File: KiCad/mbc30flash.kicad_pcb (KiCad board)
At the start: 2 copper layers, 51 x 60.2 mm, 19 parts, among them U0 CartBus, U1 BA6129AF, U2 74LVC1G332GW,125, Y1 Crystal

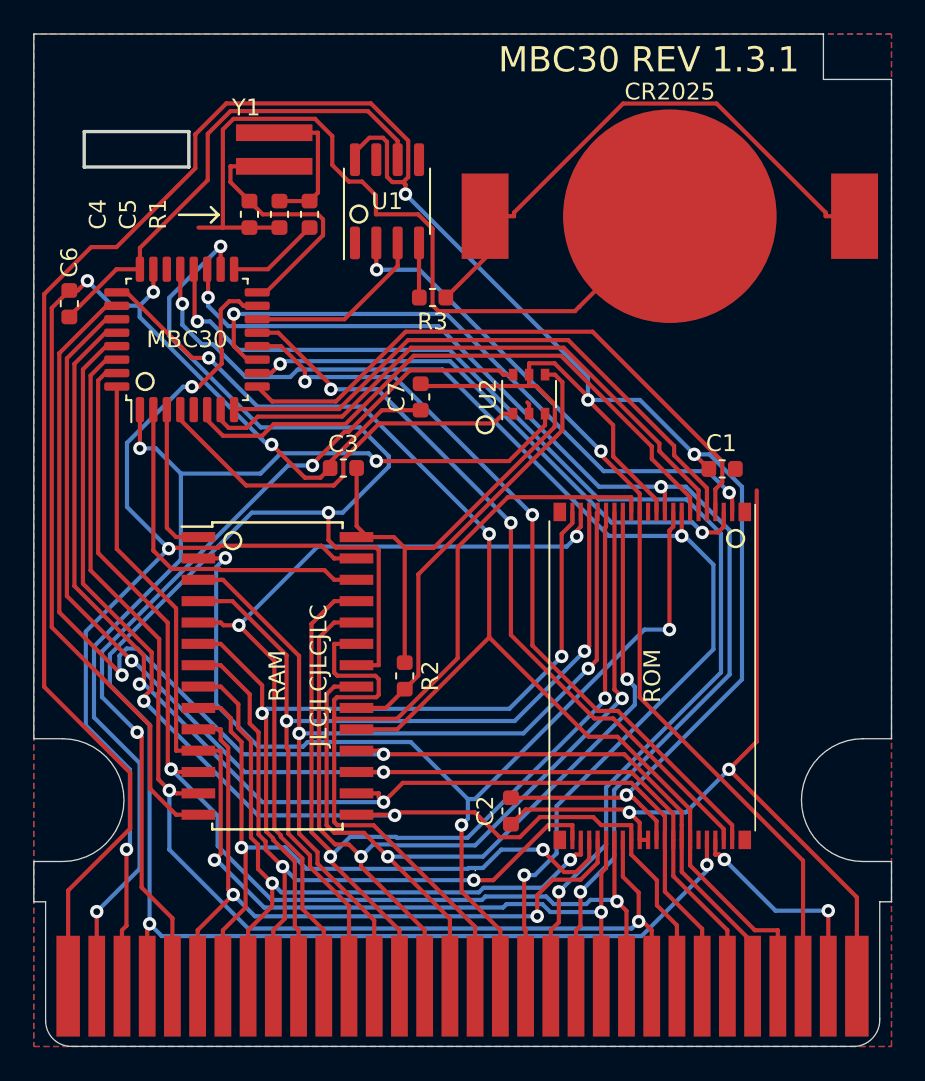
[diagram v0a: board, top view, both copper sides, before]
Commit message: Revision 1.4
- Switched cart bus footprint to [djedditt's replica of an original one](https://github.com/djedditt/kicad-gamepaks)

- Replaced the flash chip footprint with a TSOP-40 footprint.

- Redid the ground plane by hand, it should now look much better.

- Moved the battery receptacle footprint 0.5mm to the left.

- Renamed Y1 to X1

- Removed JLCJLCJLC marking for OSHPark project.

- Cleaned up schematic, it should now be much more readable.
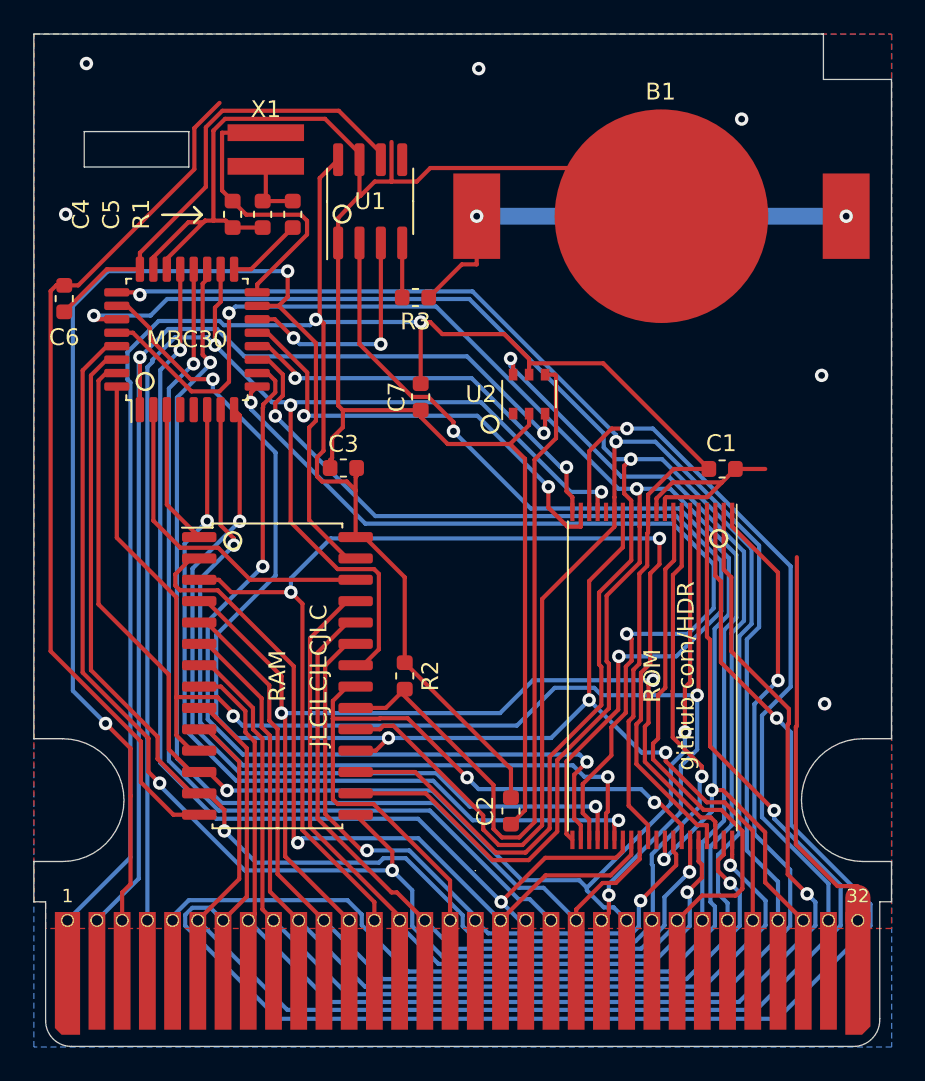
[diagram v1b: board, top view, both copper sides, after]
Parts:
- removed the ROM at (101.7, 108.0)
- removed Y1: Crystal, Custom:Resonator_SMD_muRata_CDSCB-2pin_4.5x2.0mm_HandSoldering
- added ROM: AM29F032/MBM29F033C, Custom:AM29F032-MBM29F033C, F.Cu at (101.7, 108.0)
- added X1: Crystal, Custom:Resonator_SMD_muRata_CDSCB-2pin_4.5x2.0mm_HandSoldering, F.Cu at (78.7, 76.7)
- R1: value 300Kohm -> 330K
- R2: value 10 Kohm -> 10K
- R3: value 1 Kohm -> 1K
- U0: footprint Custom:GBBus -> Connector_GameBoy:GameBoy_GamePak_CGB-002_P1.50mm_Edge
- moved G*** 31.9 mm to (90.4, 99.9)
- moved U0 24.3 mm to (90.4, 120.6)
- moved R3 1.02 mm to (87.6, 85.5)
- moved C4 1.00 mm to (76.7, 80.5)
- moved C5 1.00 mm to (78.5, 80.5)
- moved R1 1.00 mm to (80.3, 80.5)
- moved U1 1.00 mm to (84.9, 79.7)
- moved B1 0.50 mm to (102.2, 80.6)
- moved C6 0.43 mm to (66.7, 85.5)
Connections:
- MBC30 pad 4: \RAMCS -> Net-(U1-Pad4)
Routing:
- net A1: track 42.8 -> 91.8 mm, vias 2 -> 1
- net VCC: track 193.8 -> 151.4 mm, vias 4 -> 2
- net A0: track 43.4 -> 84.0 mm, vias 2 -> 1
- net A2: track 41.4 -> 80.7 mm, vias 2 -> 1
- net A3: track 42.1 -> 78.8 mm, vias 2 -> 1
- net D5: track 72.7 -> 109.3 mm
- net D4: track 72.6 -> 108.4 mm
- net D7: track 74.1 -> 107.9 mm
- net GND: track 168.4 -> 201.1 mm, vias 5 -> 6
- net D3: track 70.4 -> 101.1 mm
- net WE_AUDIO: track 13.5 -> 42.9 mm, vias 2 -> 1
- net \RD: track 116.5 -> 90.4 mm, vias 4 -> 3
- net CS: track 53.2 -> 79.2 mm, vias 2 -> 1
- net \RAMCS: track 24.4 -> 0.00 mm
- net RA20: track 46.1 -> 24.4 mm
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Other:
- board text added: "MBC30 REV 1.4"
- board text added: "github.com/HDR"
- board text removed: "CR2025"
- board text removed: "MBC30 REV 1.3.1"

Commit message: 1.4.1
- Fixed missing trace for Ram_CS
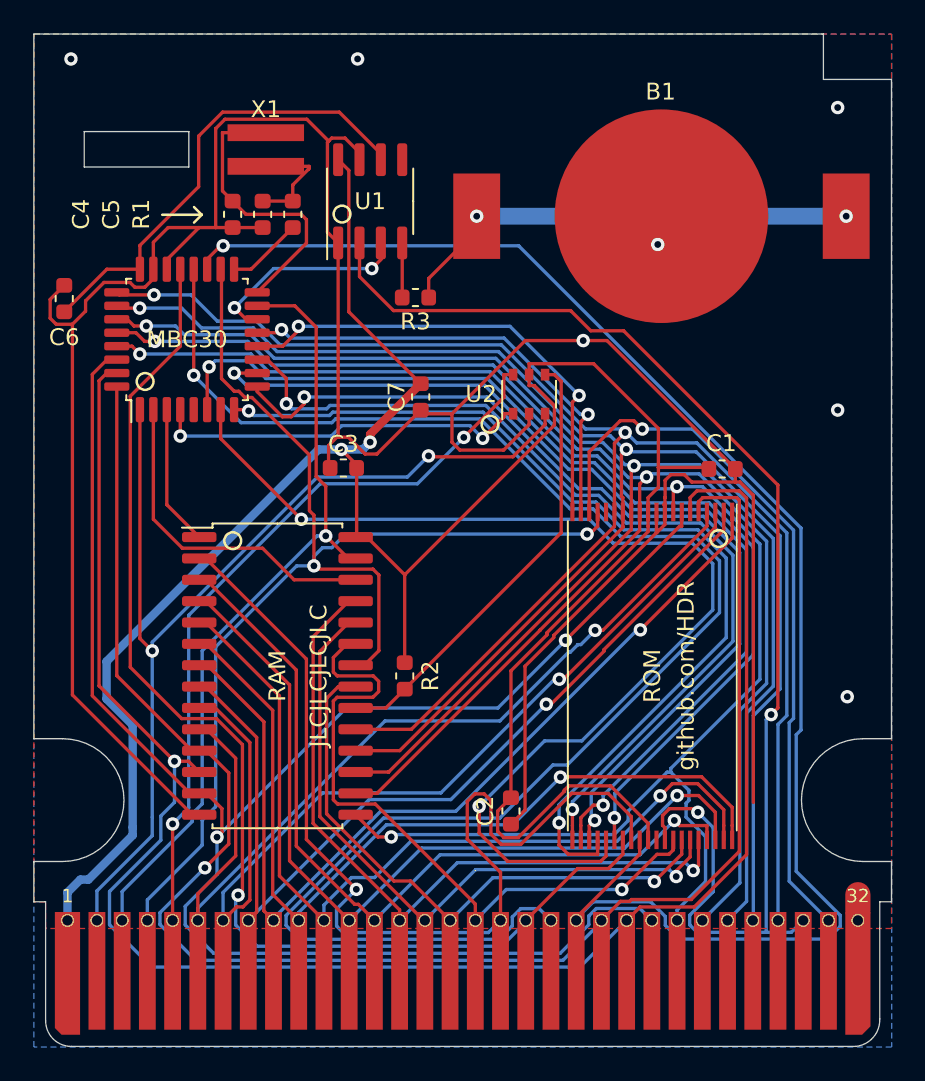
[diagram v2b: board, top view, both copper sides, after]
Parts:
- removed G***: LOGO, Custom:Suicune-Back-Silkscreen
- added Art2: 90,412581|99,90646 | Suicune, Custom:Suicune-Back-Silkscreen, B.Cu at (90.4, 99.9)
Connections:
- MBC30 pad 4: Net-(U1-Pad4) -> \RAMCS
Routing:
- net A14: track 56.5 -> 96.7 mm
- net A1: track 91.8 -> 56.2 mm
- net CS: track 79.2 -> 44.6 mm, vias 1 -> 2
- net A0: track 84.0 -> 54.7 mm
- net A15: track 64.7 -> 92.2 mm
- net A2: track 80.7 -> 54.8 mm
- net \WR: track 72.9 -> 47.2 mm, vias 2 -> 1
- net D1: track 81.4 -> 106.2 mm, vias 2 -> 1
- net A7: track 71.6 -> 48.1 mm, vias 2 -> 1
- net A3: track 78.8 -> 55.6 mm
- net \RAMCS: track 0.00 -> 22.7 mm, vias 0 -> 2
- net #CE: track 44.5 -> 26.7 mm
- net RA15: track 49.1 -> 66.5 mm
- net D2: track 88.8 -> 105.5 mm
- net D0: track 83.5 -> 99.1 mm, vias 3 -> 1
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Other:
- net class Default: trace_width 0.25 -> 0.2
- board text added: "MBC30 REV 1.4.1"
- board text removed: "MBC30 REV 1.4"

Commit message: 1.4.2
- Fixed a symbol kicad "rescued" causing the pinout to be backwards (this put the chip direction indicator in the wrong corner)
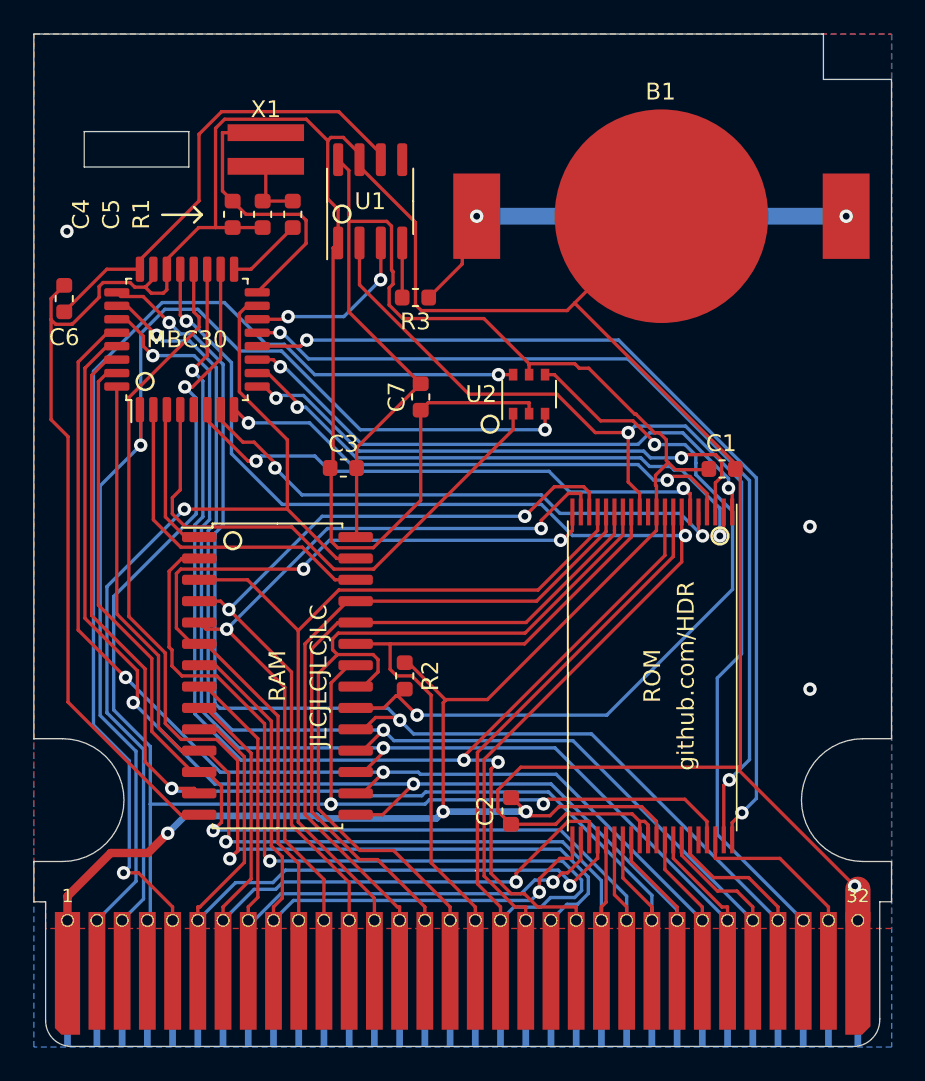
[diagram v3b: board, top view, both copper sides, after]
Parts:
- removed Art2: 90,412581|99,90646 | Suicune, Custom:Suicune-Back-Silkscreen
- added Art1: 90,412581|99,90646 | Crystal Clear, Custom:Suicune-Back-Silkscreen, B.Cu at (90.4, 99.9)
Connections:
- ROM pad 1: A3 -> RA19
- ROM pad 10: GND -> VCC
- ROM pad 11: VCC -> Net-(U4-Pad11)
- ROM pad 12: D4 -> RESET
- ROM pad 13: D5 -> A11
- ROM pad 14: D6 -> A10
- ROM pad 15: D7 -> A9
- ROM pad 16: Net-(U4-Pad16) -> A8
- ROM pad 17: \RD -> A7
- ROM pad 18: WE_AUDIO -> A6
- ROM pad 19: RA21 -> A5
- ROM pad 2: A2 -> RA18
- ROM pad 20: RA20 -> A4
- ROM pad 21: RA19 -> A3
- ROM pad 22: RA18 -> A2
- ROM pad 23: RA17 -> A1
- ROM pad 24: RA16 -> A0
- ROM pad 25: RA15 -> D0
- ROM pad 26: RA14 -> D1
- ROM pad 27: A13 -> D2
- ROM pad 28: A12 -> D3
- ROM pad 29: A15 -> GND
- ROM pad 3: A1 -> RA17
- ROM pad 30: VCC -> GND
- ROM pad 31: Net-(U4-Pad31) -> VCC
- ROM pad 32: RESET -> D4
- ROM pad 33: A11 -> D5
- ROM pad 34: A10 -> D6
- ROM pad 35: A9 -> D7
- ROM pad 36: A8 -> Net-(U4-Pad36)
- ROM pad 37: A7 -> \RD
- ROM pad 38: A6 -> WE_AUDIO
- ROM pad 39: A5 -> RA21
- ROM pad 4: A0 -> RA16
- ROM pad 40: A4 -> RA20
- ROM pad 5: D0 -> RA15
- ROM pad 6: D1 -> RA14
- ROM pad 7: D2 -> A13
- ROM pad 8: D3 -> A12
- ROM pad 9: GND -> A15
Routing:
- net D1: track 106.2 -> 64.5 mm
- net D0: track 99.1 -> 61.3 mm
- net D2: track 105.5 -> 68.5 mm, vias 2 -> 1
- net WE_AUDIO: track 43.5 -> 9.82 mm, vias 1 -> 0
- net RA15: track 66.5 -> 33.8 mm
- net A14: track 96.7 -> 67.1 mm
- net RA14: track 60.5 -> 32.7 mm
- net GND: track 185.8 -> 212.9 mm, vias 7 -> 4
- net RA21: track 27.8 -> 54.9 mm
- net RA20: track 28.6 -> 55.3 mm
- net RA16: track 57.6 -> 31.5 mm
- net D4: track 94.8 -> 71.1 mm
- net RA18: track 57.9 -> 34.2 mm
- net RA17: track 55.1 -> 32.9 mm
- net D5: track 94.6 -> 72.7 mm
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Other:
- board text added: "MBC30 REV 1.4.2"
- board text removed: "MBC30 REV 1.4.1"
